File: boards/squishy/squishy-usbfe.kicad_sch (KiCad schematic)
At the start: 21 parts, among them J1 USB_C_Receptacle, U1 LFE5UM5G-45F-8BG381C, U13 HD3SS460, U14 TPD4E02B04DQA, U15 TPD4E02B04DQA, U17 USB3318, U3 CYPD3174-24, U4 SP3400-02UTG, X2 13MHz

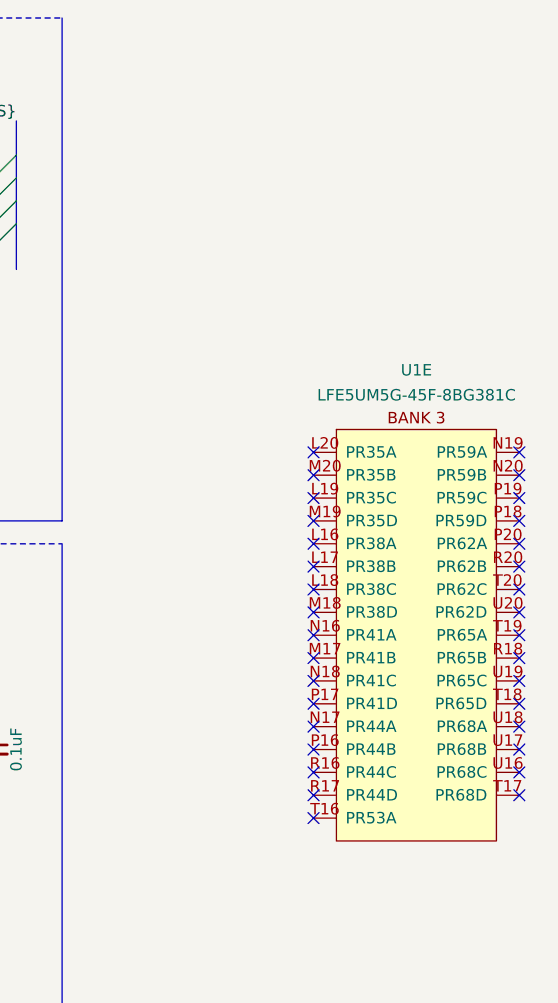
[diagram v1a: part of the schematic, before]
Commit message: hardware: squishy: replaced the SPI flash with a less batshit device from GigaDevice
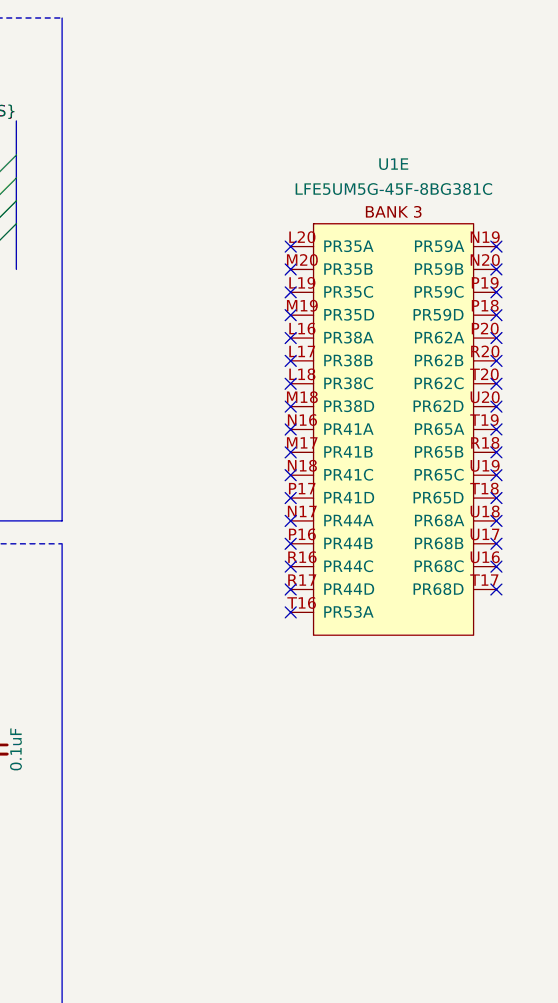
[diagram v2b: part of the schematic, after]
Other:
- moved on the sheet: U1E
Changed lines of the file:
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@@
   (no_connect (at 82.55 161.29))
   (no_connect (at 82.55 163.83))
-  (no_connect (at 278.13 102.87))
-  (no_connect (at 278.13 100.33))
-  (no_connect (at 278.13 62.23))
-  (no_connect (at 300.99 62.23))
-  (no_connect (at 300.99 64.77))
-  (no_connect (at 300.99 92.71))
-  (no_connect (at 300.99 95.25))
-  (no_connect (at 300.99 97.79))
-  (no_connect (at 300.99 100.33))
-  (no_connect (at 300.99 67.31))
-  (no_connect (at 300.99 69.85))
-  (no_connect (at 300.99 72.39))
-  (no_connect (at 300.99 74.93))
-  (no_connect (at 300.99 77.47))
-  (no_connect (at 300.99 80.01))
-  (no_connect (at 300.99 82.55))
-  (no_connect (at 300.99 85.09))
-  (no_connect (at 300.99 87.63))
-  (no_connect (at 300.99 90.17))
+  (no_connect (at 275.59 80.01))
+  (no_connect (at 275.59 77.47))
+  (no_connect (at 275.59 39.37))
+  (no_connect (at 298.45 39.37))
+  (no_connect (at 298.45 41.91))
+  (no_connect (at 298.45 69.85))
+  (no_connect (at 298.45 72.39))
+  (no_connect (at 298.45 74.93))
+  (no_connect (at 298.45 77.47))
+  (no_connect (at 298.45 44.45))
+  (no_connect (at 298.45 46.99))
+  (no_connect (at 298.45 49.53))
+  (no_connect (at 298.45 52.07))
+  (no_connect (at 298.45 54.61))
+  (no_connect (at 298.45 57.15))
+  (no_connect (at 298.45 59.69))
+  (no_connect (at 298.45 62.23))
+  (no_connect (at 298.45 64.77))
+  (no_connect (at 298.45 67.31))
   (no_connect (at 118.11 64.77))
   (no_connect (at 118.11 69.85))
@@
   (no_connect (at 82.55 151.13))
   (no_connect (at 205.74 111.76))
-  (no_connect (at 278.13 97.79))
-  (no_connect (at 278.13 95.25))
-  (no_connect (at 278.13 92.71))
-  (no_connect (at 278.13 90.17))
-  (no_connect (at 278.13 87.63))
-  (no_connect (at 278.13 85.09))
-  (no_connect (at 278.13 82.55))
-  (no_connect (at 278.13 80.01))
-  (no_connect (at 278.13 77.47))
-  (no_connect (at 278.13 74.93))
-  (no_connect (at 278.13 72.39))
-  (no_connect (at 278.13 69.85))
-  (no_connect (at 278.13 67.31))
-  (no_connect (at 278.13 64.77))
+  (no_connect (at 275.59 74.93))
+  (no_connect (at 275.59 72.39))
+  (no_connect (at 275.59 69.85))
+  (no_connect (at 275.59 67.31))
+  (no_connect (at 275.59 64.77))
+  (no_connect (at 275.59 62.23))
+  (no_connect (at 275.59 59.69))
+  (no_connect (at 275.59 57.15))
+  (no_connect (at 275.59 54.61))
+  (no_connect (at 275.59 52.07))
+  (no_connect (at 275.59 49.53))
+  (no_connect (at 275.59 46.99))
+  (no_connect (at 275.59 44.45))
+  (no_connect (at 275.59 41.91))
   (no_connect (at 82.55 168.91))
   (no_connect (at 201.93 45.72))
@@
     (pin "1")
   )
-  (symbol (lib_id "lethalbit:LFE5UM5G-45F-8BG381C") (at 289.56 62.23 0) (unit 5)
-    (in_bom yes) (on_board yes)
-    (property "Reference" "U1" (id 0) (at 289.56 53.1049 0))
-    (property "Value" "LFE5UM5G-45F-8BG381C" (id 1) (at 289.56 55.88 0))
-    (property "Footprint" "lethalbit:318caBGA" (id 2) (at 289.56 46.99 0)
-      (effects (font (size 1.27 1.27)) hide)
-    )
-    (property "Datasheet" "https://www.latticesemi.com/view_document?document_id=50461" (id 3) (at 289.56 109.22 0)
-      (effects (font (size 1.27 1.27)) hide)
-    )
-    (property "MFR" "Lattice" (id 4) (at 289.56 49.53 0)
-      (effects (font (size 1.27 1.27)) hide)
-    )
-    (property "MPN" "LFE5UM5G-45F-8BG381C" (id 5) (at 289.56 53.34 0)
-      (effects (font (size 1.27 1.27)) hide)
-    )
+  (symbol (lib_id "lethalbit:LFE5UM5G-45F-8BG381C") (at 287.02 39.37 0) (unit 5)
+    (in_bom yes) (on_board yes)
+    (property "Reference" "U1" (id 0) (at 287.02 30.2449 0))
+    (property "Value" "LFE5UM5G-45F-8BG381C" (id 1) (at 287.02 33.02 0))
+    (property "Footprint" "lethalbit:318caBGA" (id 2) (at 287.02 24.13 0)
+      (effects (font (size 1.27 1.27)) hide)
+    )
+    (property "Datasheet" "https://www.latticesemi.com/view_document?document_id=50461" (id 3) (at 287.02 86.36 0)
+      (effects (font (size 1.27 1.27)) hide)
+    )
+    (property "MFR" "Lattice" (id 4) (at 287.02 26.67 0)
+      (effects (font (size 1.27 1.27)) hide)
+    )
+    (property "MPN" "LFE5UM5G-45F-8BG381C" (id 5) (at 287.02 30.48 0)
+      (effects (font (size 1.27 1.27)) hide)
+    )

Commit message: hardware: squishy: some footprint/part updates and cleanup
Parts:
- X2: footprint Oscillator:Oscillator_SMD_Abracon_ASE-4Pin_3.2x2.5mm -> rhais_osc:SMD3225
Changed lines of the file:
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@@
       (effects (font (size 1.27 1.27)) (justify left))
     )
-    (property "Footprint" "Oscillator:Oscillator_SMD_Abracon_ASE-4Pin_3.2x2.5mm" (id 2) (at 130.81 138.43 0)
+    (property "Footprint" "rhais_osc:SMD3225" (id 2) (at 130.81 138.43 0)
       (effects (font (size 1.27 1.27)) hide)
     )

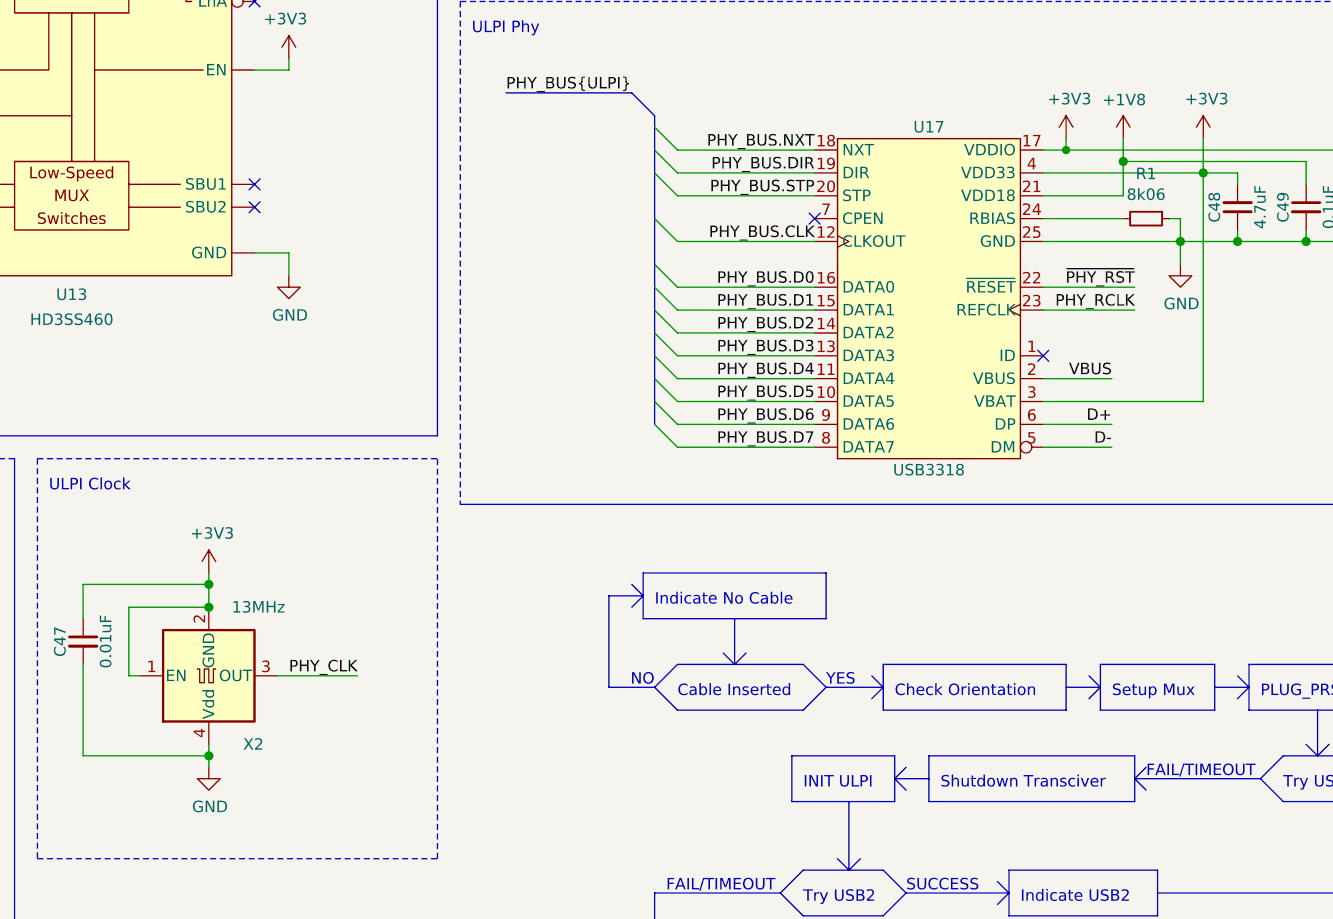
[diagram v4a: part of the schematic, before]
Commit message: hardware: squishy: usb fe: fixing up and getting the last little bits of the USB front end done and dusted, just needs power routing now
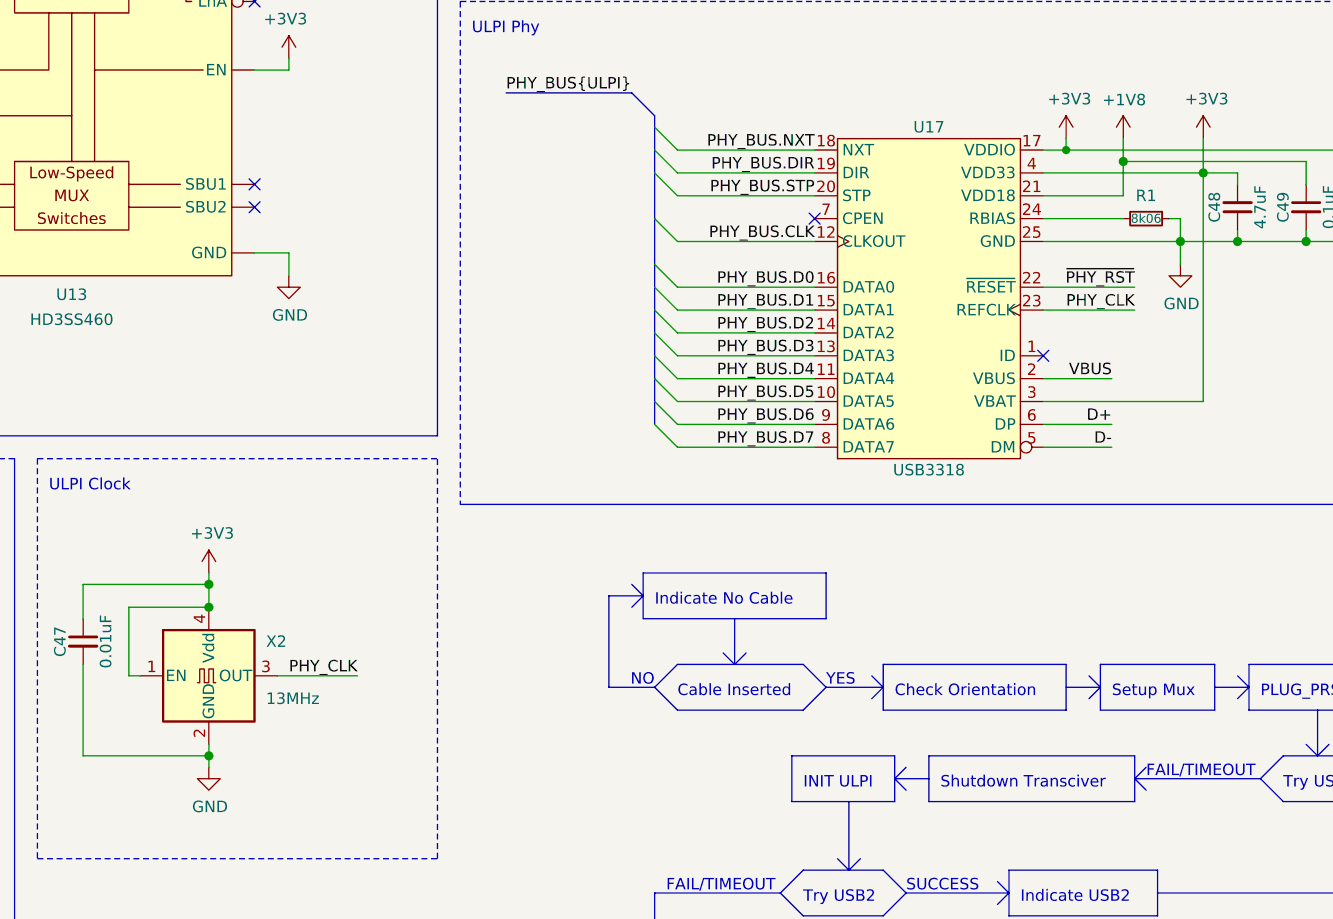
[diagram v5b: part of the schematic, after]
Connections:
- net PHY_RCLK is gone; now on net PHY_CLK: U17.23 (REFCLK)
- net +3V3: now also X2.4 (Vdd); no longer X2.2 (GND)
- net GND: now also X2.2 (GND); no longer X2.4 (Vdd)
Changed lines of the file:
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@@
     (effects (font (size 1.27 1.27)) (justify right bottom))
   )
-  (label "PHY_RCLK" (at 215.9 106.68 180)
+  (label "PHY_CLK" (at 215.9 106.68 180)
     (effects (font (size 1.27 1.27)) (justify right bottom))
   )
@@
   (symbol (lib_id "Device:R_Small") (at 217.17 96.52 270) (unit 1)
     (in_bom yes) (on_board yes)
-    (property "Reference" "R1" (id 0) (at 217.17 91.5416 90))
-    (property "Value" "8k06" (id 1) (at 217.17 93.853 90))
+    (property "Reference" "R1" (id 0) (at 217.17 93.98 90))
+    (property "Value" "8k06" (id 1) (at 217.17 96.52 90)
+      (effects (font (size 1 1)))
+    )
     (property "Footprint" "Resistor_SMD:R_0603_1608Metric" (id 2) (at 217.17 96.52 0)
       (effects (font (size 1.27 1.27)) hide)
@@
     (pin "1")
   )
-  (symbol (lib_id "Oscillator:ASE-xxxMHz") (at 113.03 147.32 0) (mirror x) (unit 1)
-    (in_bom yes) (on_board yes)
-    (property "Reference" "X2" (id 0) (at 116.84 154.94 0)
-      (effects (font (size 1.27 1.27)) (justify left))
-    )
-    (property "Value" "13MHz" (id 1) (at 115.57 139.7 0)
-      (effects (font (size 1.27 1.27)) (justify left))
-    )
-    (property "Footprint" "rhais_osc:SMD3225" (id 2) (at 130.81 138.43 0)
-      (effects (font (size 1.27 1.27)) hide)
-    )
+  (symbol (lib_id "Oscillator:ASE-xxxMHz") (at 113.03 147.32 0) (unit 1)
+    (in_bom yes) (on_board yes)
+    (property "Reference" "X2" (id 0) (at 119.38 143.51 0)
+      (effects (font (size 1.27 1.27)) (justify left))
+    )
+    (property "Value" "13MHz" (id 1) (at 119.38 149.86 0)
+      (effects (font (size 1.27 1.27)) (justify left))
+    )
+    (property "Footprint" "rhais_osc:SMD3225" (id 2) (at 130.81 156.21 0)
+      (effects (font (size 1.27 1.27)) hide)
+    )

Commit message: hardware: fixed the USB PD controller pinout, as well as the AT SAMD symbol
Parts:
- U3: symbol DX-MON-NG:CYPD3174-24 -> DX-MON:CYPD3174-24; MFR Cypress -> (property "Reference" "U" (id 0) (at -17.78 21.59 0); MPN CYPD3174-24LQXQ -> (effects (font (size 1.27 1.27)) (justify left)); OC_FARNELL 2896248 -> ); URL_FARNELL https://uk.farnell.com/cypress-semiconductor/cypd3174-24lqx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 -> (property "Value" "CYPD3174-24" (id 1) (at 17.78 -21.59 0)
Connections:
- net GND: now also U3.22 (GND)
